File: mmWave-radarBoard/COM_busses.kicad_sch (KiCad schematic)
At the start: 31 parts, among them J401 Conn_01x03_Socket, J402 Conn_01x03_Socket, J403 Conn_01x03_Socket, U401 TCAN1042HGVDRQ1, U402 TLIN1039DDFRQ1, U403 TRS3221EIDBR

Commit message: Updated schematic
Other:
- company: Emiel V -> Designer: EV
- moved on the sheet: C401, C402, C403, C404, C405, C406, C407, C408, C409, C410, D208, D401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

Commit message: Finished schematic
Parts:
- C401: renamed from C403; footprint (none) -> Capacitor_SMD:C_0603_1608Metric
- C402, C404: footprint (none) -> Capacitor_SMD:C_0603_1608Metric
- C403: renamed from C401; footprint (none) -> Capacitor_SMD:C_0805_2012Metric
- C405: footprint (none) -> Capacitor_SMD:C_0805_2012Metric
- C406: renamed from C409; footprint (none) -> Capacitor_SMD:C_0603_1608Metric
- C407: renamed from C410; footprint (none) -> Capacitor_SMD:C_0603_1608Metric
- C408: renamed from C407; footprint (none) -> Capacitor_SMD:C_0603_1608Metric
- C409: renamed from C406; footprint (none) -> Capacitor_SMD:C_0603_1608Metric
- C410: renamed from C408; footprint (none) -> Capacitor_SMD:C_0603_1608Metric
- J401, J402, J403: footprint (none) -> Connector_JST:JST_ZE_B03B-ZESK-D_1x03_P1.50mm_Vertical
- R401: renamed from R261; footprint (none) -> Resistor_SMD:R_0402_1005Metric
- R402: renamed from R264; footprint (none) -> Resistor_SMD:R_0402_1005Metric
- R403: renamed from R260; footprint (none) -> Resistor_SMD:R_0402_1005Metric
- R404: renamed from R259; footprint (none) -> Resistor_SMD:R_0402_1005Metric
- R405: renamed from R265; footprint (none) -> Resistor_SMD:R_0402_1005Metric
- R406: renamed from R262; footprint (none) -> Resistor_SMD:R_0402_1005Metric
- R407: renamed from R263; footprint (none) -> Resistor_SMD:R_0402_1005Metric
- R408: renamed from R266; footprint (none) -> Resistor_SMD:R_0805_2012Metric
- R409: renamed from R271; footprint (none) -> Resistor_SMD:R_0402_1005Metric
- R410: renamed from R270; footprint (none) -> Resistor_SMD:R_0402_1005Metric
- R411: renamed from R267; footprint (none) -> Resistor_SMD:R_0402_1005Metric
- R412: renamed from R268; footprint (none) -> Resistor_SMD:R_0402_1005Metric
- R413: renamed from R269; footprint (none) -> Resistor_SMD:R_0402_1005Metric
- renumbered D208 to D401, D401 to D402

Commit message: Updated radar PCB and schematic
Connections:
- net RS232_RX: now also U403.8 (RIN); no longer U403.9 (ROUT)
- net LIN: now reaches C405.2, J402.2 (Pin_2), R408.1, U402.6 (LIN)
- net TX: now reaches D402.1 (K), J403.1 (Pin_1), U403.13 (DOUT)
- net RX: now reaches D402.2 (K), J403.3 (Pin_3)
- net RX: now also U403.9 (ROUT); no longer U403.8 (RIN)

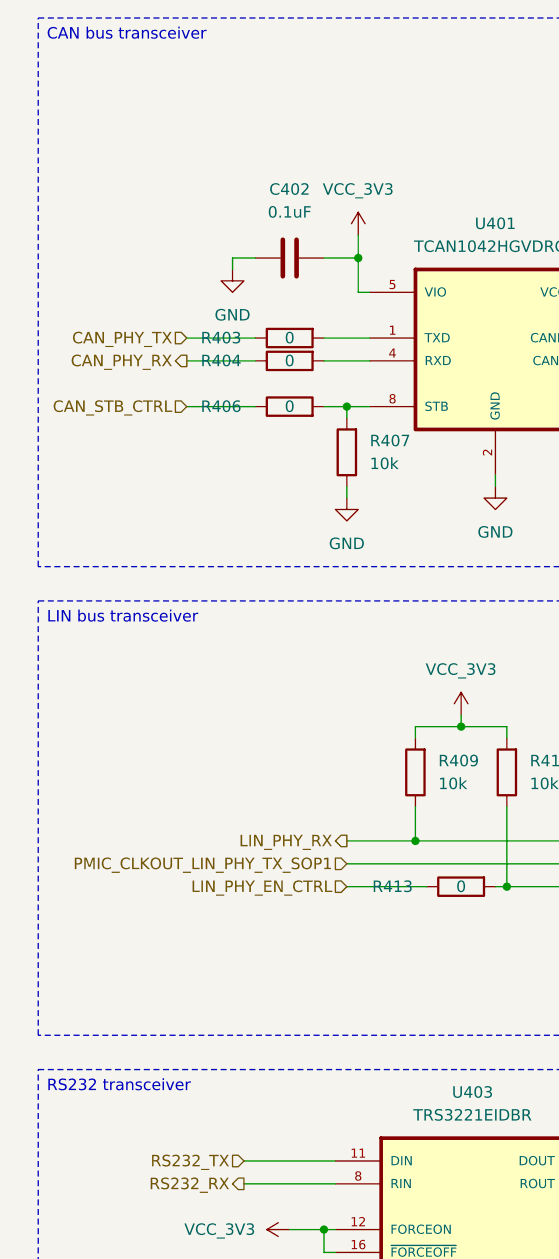
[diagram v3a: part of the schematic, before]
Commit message: Updated schematic and PCB
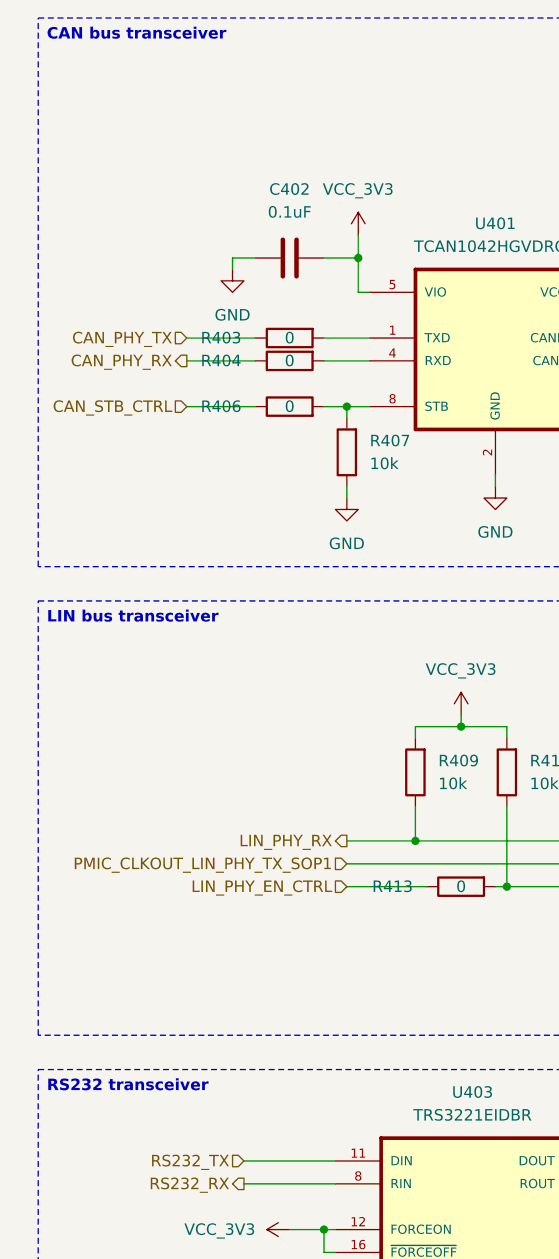
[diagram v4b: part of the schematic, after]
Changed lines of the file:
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@@
 	(title_block
 		(title "Communication busses")
-		(date "2025-04-13")
+		(date "2025-04-20")
 		(rev "V1.0")
 		(company "Designer: EV")
@@
 			(font
 				(size 1.27 1.27)
+				(thickness 0.254)
+				(bold yes)
 			)
 			(justify left top)
@@
 			(font
 				(size 1.27 1.27)
+				(thickness 0.254)
+				(bold yes)
 			)
 			(justify left top)
@@
 			(font
 				(size 1.27 1.27)
+				(thickness 0.254)
+				(bold yes)
 			)
 			(justify left top)

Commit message: Updated schematic and layout PCB
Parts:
- renumbered C401 to C80, C402 to C81, C403 to C82, C404 to C83, C405 to C84, C406 to C85, C407 to C86, C408 to C87, C409 to C88, C410 to C89, D401 to D8, D402 to D9, J401 to J6, J402 to J7, J403 to J8, R401 to R47, R402 to R48, R403 to R49, R404 to R50, R405 to R51, R406 to R52, R407 to R53, R408 to R54, R409 to R55, R410 to R56, R411 to R57, R412 to R58, R413 to R59, U402 to U10, U403 to U11, U401 to U9
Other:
- title: Communication busses -> Power
